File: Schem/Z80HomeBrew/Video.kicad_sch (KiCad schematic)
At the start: 39 parts, among them J7 RCA GREEN (Y), J8 RCA RED (Pr), J9 RCA BLUE (Pb), U13 SN74HCT574DWR, U21 SN74HCT574DWR, U22 TMS9928A, U23 THS7314DR, U24 AS7C256A-10TCN, U25 SN74LVC1G19DCKR, U26 SN74HC273DWR, U27 SN74HCT574DWR, U28 CD74HC139M96, U29 SN74HCT04DR, Y4 MP107-E

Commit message: Completed schematics
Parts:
- removed J7: RCA GREEN (Y), Connector_Coaxial:SMA_Amphenol_132289_EdgeMount, symbol Connector:Conn_Coaxial
- removed J8: RCA RED (Pr), Connector_Coaxial:SMA_Amphenol_132289_EdgeMount, symbol Connector:Conn_Coaxial
- removed J9: RCA BLUE (Pb), Connector_Coaxial:SMA_Amphenol_132289_EdgeMount, symbol Connector:Conn_Coaxial
- added D5, D6: BAT54J, Diode_SMD:D_SOD-323F, symbol Diode:BAT54J
- added J10: RCJ-32265, Footprints:RCJ-32234, symbol RCJ-32265:RCJ-32265
- U24: footprint TSOP-28_8X13P4_ALL -> Footprints:TSOP-28_8X13P4_ALL
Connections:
- net GND: now also J10.1, J10.3, J10.5
- net ~{INT}: now also D6.2 (A); no longer U25.4 (Y1)
- net ~{NMI}: now also D5.2 (A); no longer U25.6 (Y0)
- net at C46.2: now also J10.4
- net at C50.2: now also J10.6
- net at C43.2: now also J10.2
- new net: D6.1 (K), U25.4 (Y1)
- new net: D5.1 (K), U25.6 (Y0)
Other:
- note added: "BLUE (Pb)"
- note added: "RED (Pr)"
- moved on the sheet: U29C, U29D, U29E

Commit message: Finally found a name "Zephyr-80" for the brew and committing the first pbc
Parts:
- added J11, J12, J8: Conn_01x02_Pin, Connector_PinHeader_2.54mm:PinHeader_1x02_P2.54mm_Vertical, symbol Connector:Conn_01x02_Pin
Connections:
- net GND: now also J11.2 (Pin_2), J12.2 (Pin_2), J8.2 (Pin_2)
- net at C43.2, J10.2: now also J8.1 (Pin_1)
- net at C46.2, J10.4: now also J11.1 (Pin_1)
- net at C50.2, J10.6: now also J12.1 (Pin_1)
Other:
- note added: "Pin Headers as alternative to RCA Jack"

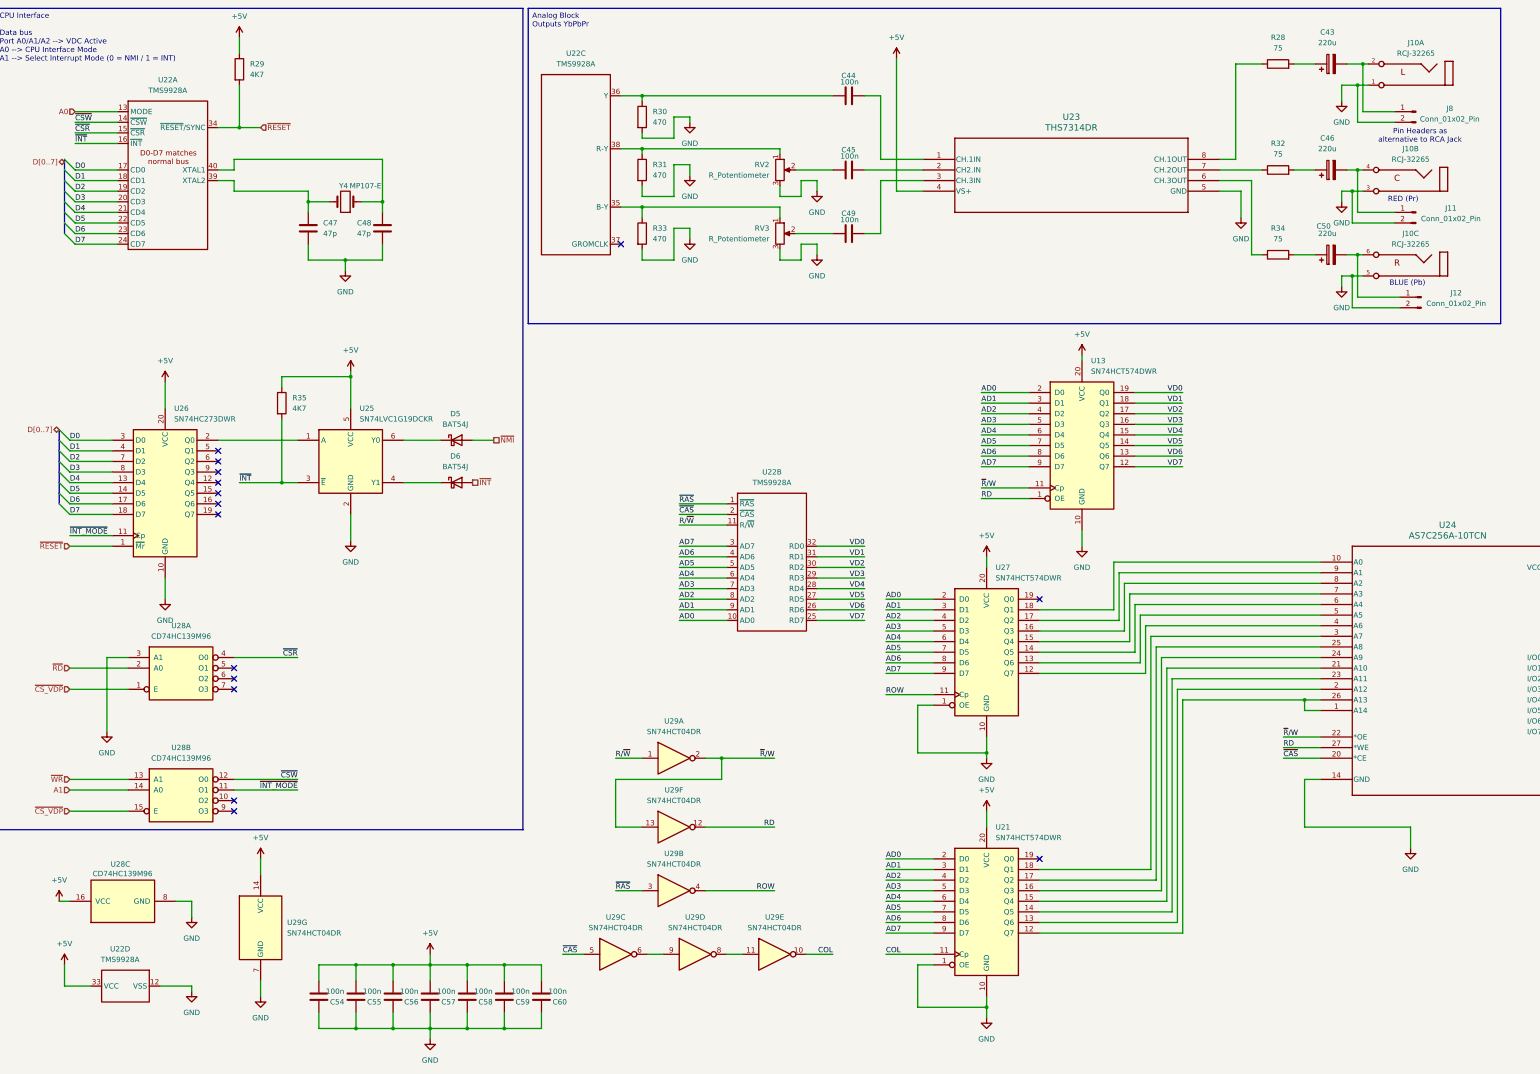
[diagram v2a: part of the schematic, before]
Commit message: Added pBITzBackplane and MezzanineConnector
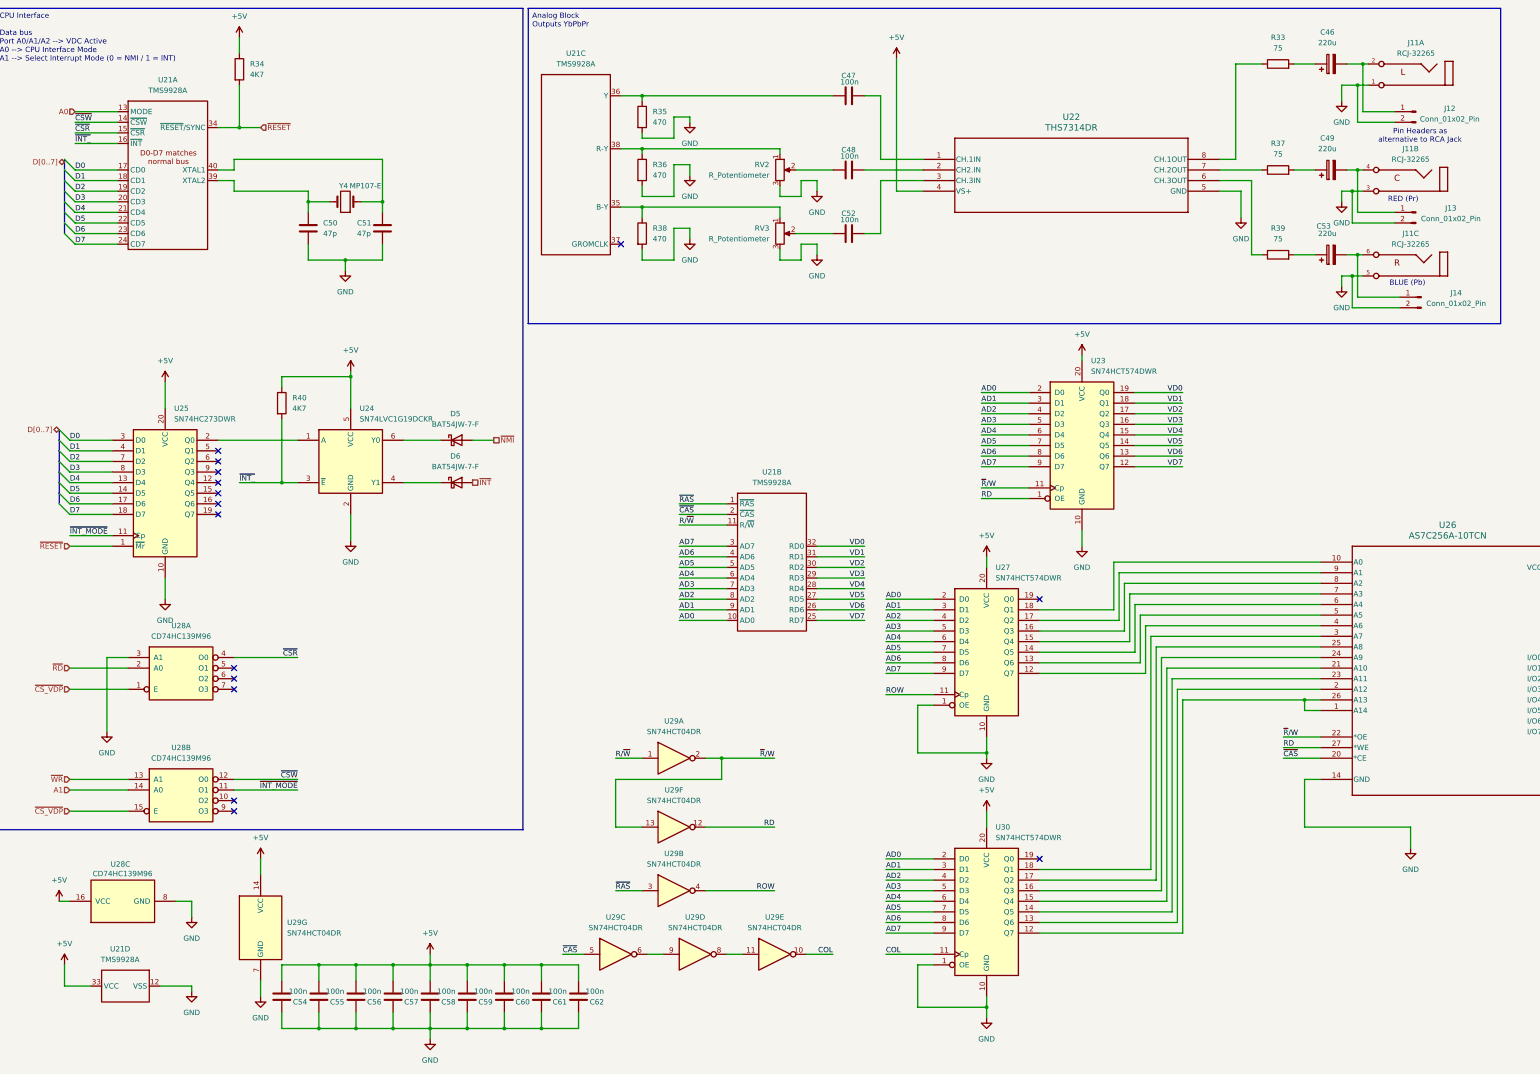
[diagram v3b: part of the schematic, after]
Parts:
- added C54, C62: 100n, Capacitor_SMD:C_0603_1608Metric, symbol Device:C
- C46: renamed from C43; footprint Capacitor_Tantalum_SMD:CP_EIA-3528-21_Kemet-B -> Capacitor_THT:CP_Radial_D6.3mm_P2.50mm; MANUFACTURER_PART_NUMBER (none) -> 16ZLH220MEFCT16.3X11
- C47: renamed from C44; MANUFACTURER_PART_NUMBER (none) -> C0603C104K5RACTU
- C48: renamed from C45; MANUFACTURER_PART_NUMBER (none) -> C0603C104K5RACTU
- C49: renamed from C46; footprint Capacitor_Tantalum_SMD:CP_EIA-3528-21_Kemet-B -> Capacitor_THT:CP_Radial_D6.3mm_P2.50mm; MANUFACTURER_PART_NUMBER (none) -> 16ZLH220MEFCT16.3X11
- C50: renamed from C47; MANUFACTURER_PART_NUMBER (none) -> 885012006021
- C51: renamed from C48; MANUFACTURER_PART_NUMBER (none) -> 885012006021
- C52: renamed from C49; MANUFACTURER_PART_NUMBER (none) -> C0603C104K5RACTU
- C53: renamed from C50; footprint Capacitor_Tantalum_SMD:CP_EIA-3528-21_Kemet-B -> Capacitor_THT:CP_Radial_D6.3mm_P2.50mm; MANUFACTURER_PART_NUMBER (none) -> 16ZLH220MEFCT16.3X11
- C55: renamed from C54; MANUFACTURER_PART_NUMBER (none) -> C0603C104K5RACTU
- C56: renamed from C55; MANUFACTURER_PART_NUMBER (none) -> C0603C104K5RACTU
- C57: renamed from C56; MANUFACTURER_PART_NUMBER (none) -> C0603C104K5RACTU
- C58: renamed from C57; MANUFACTURER_PART_NUMBER (none) -> C0603C104K5RACTU
- C59: renamed from C58; MANUFACTURER_PART_NUMBER (none) -> C0603C104K5RACTU
- C60: renamed from C59; MANUFACTURER_PART_NUMBER (none) -> C0603C104K5RACTU
- C61: renamed from C60; MANUFACTURER_PART_NUMBER (none) -> C0603C104K5RACTU
- D5, D6: value BAT54J -> BAT54JW-7-F; MANUFACTURER_PART_NUMBER (none) -> BAT54JW-7-F
- J11: renamed from J10; MANUFACTURER_PART_NUMBER (none) -> RCJ-32265
- J12: renamed from J8; MANUFACTURER_PART_NUMBER (none) -> 732-5301-ND
- J13: renamed from J11; MANUFACTURER_PART_NUMBER (none) -> 732-5301-ND
- J14: renamed from J12; MANUFACTURER_PART_NUMBER (none) -> 732-5301-ND
- R33: renamed from R28; MANUFACTURER_PART_NUMBER (none) -> RC0603FR-0775RL
- R34: renamed from R29; MANUFACTURER_PART_NUMBER (none) -> CRCW06034K70FKEA
- R35: renamed from R30; MANUFACTURER_PART_NUMBER (none) -> RC0603JR-07470RL
- R36: renamed from R31; MANUFACTURER_PART_NUMBER (none) -> RC0603JR-07470RL
- R37: renamed from R32; MANUFACTURER_PART_NUMBER (none) -> RC0603FR-0775RL
- R38: renamed from R33; MANUFACTURER_PART_NUMBER (none) -> RC0603JR-07470RL
- R39: renamed from R34; MANUFACTURER_PART_NUMBER (none) -> RC0603FR-0775RL
- R40: renamed from R35; MANUFACTURER_PART_NUMBER (none) -> CRCW06034K70FKEA
- RV2, RV3: MANUFACTURER_PART_NUMBER (none) -> 3266W-1-103LF
- U21: renamed from U22; MANUFACTURER_PART_NUMBER (none) -> A 40-LC-TT
- U22: renamed from U23; MANUFACTURER_PART_NUMBER (none) -> THS7314DR
- U23: renamed from U13; MANUFACTURER_PART_NUMBER (none) -> SN74HCT574DWR
- U24: renamed from U25; MANUFACTURER_PART_NUMBER (none) -> SN74LVC1G19DCKR
- U25: renamed from U26; MANUFACTURER_PART_NUMBER (none) -> SN74HC273DWR
- U26: renamed from U24; MANUFACTURER_PART_NUMBER (none) -> AS7C256A-10TCN
- U27: MANUFACTURER_PART_NUMBER (none) -> SN74HCT574DWR
- U28: MANUFACTURER_PART_NUMBER (none) -> CD74HC139M96
- U29: MANUFACTURER_PART_NUMBER (none) -> SN74HCT04DR
- U30: renamed from U21; MANUFACTURER_PART_NUMBER (none) -> SN74HCT574DWR
- Y4: MANUFACTURER_PART_NUMBER (none) -> MP107-E
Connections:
- net +5V: now also C54.1, C62.1
- net GND: now also C54.2, C62.2
- net ~{INT}: no longer R40.2, U21.16 (~{INT}), U24.3 (~{E})
- new net ~{INT_}: R40.2, U21.16 (~{INT}), U24.3 (~{E})
